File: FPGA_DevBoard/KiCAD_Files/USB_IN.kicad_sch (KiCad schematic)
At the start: 14 parts, among them J14 AWHW 14G-SMD, J3 USB4105-GF-A-060, SW1 219-8MST, U12 FT4232HPQ-REEL, X2 12MHz

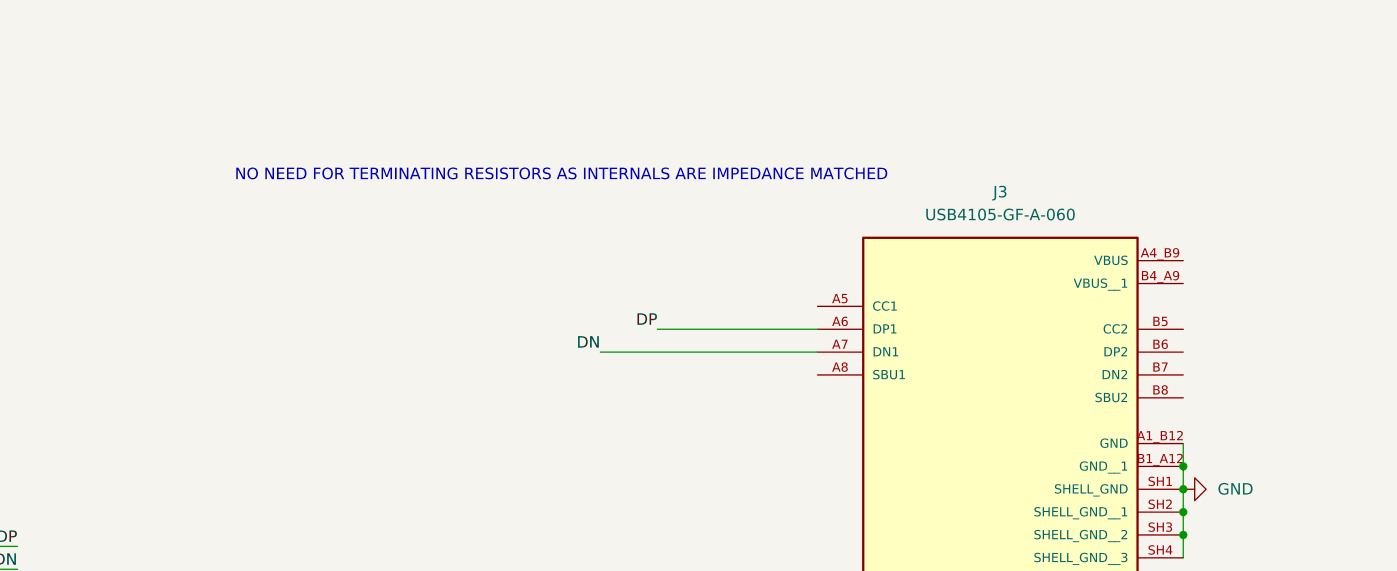
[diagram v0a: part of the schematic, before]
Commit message: ESD
Added ESD to the main USB programmer. Also added terminating resistors and test points. Also updated some planes to make sure everything was connected.
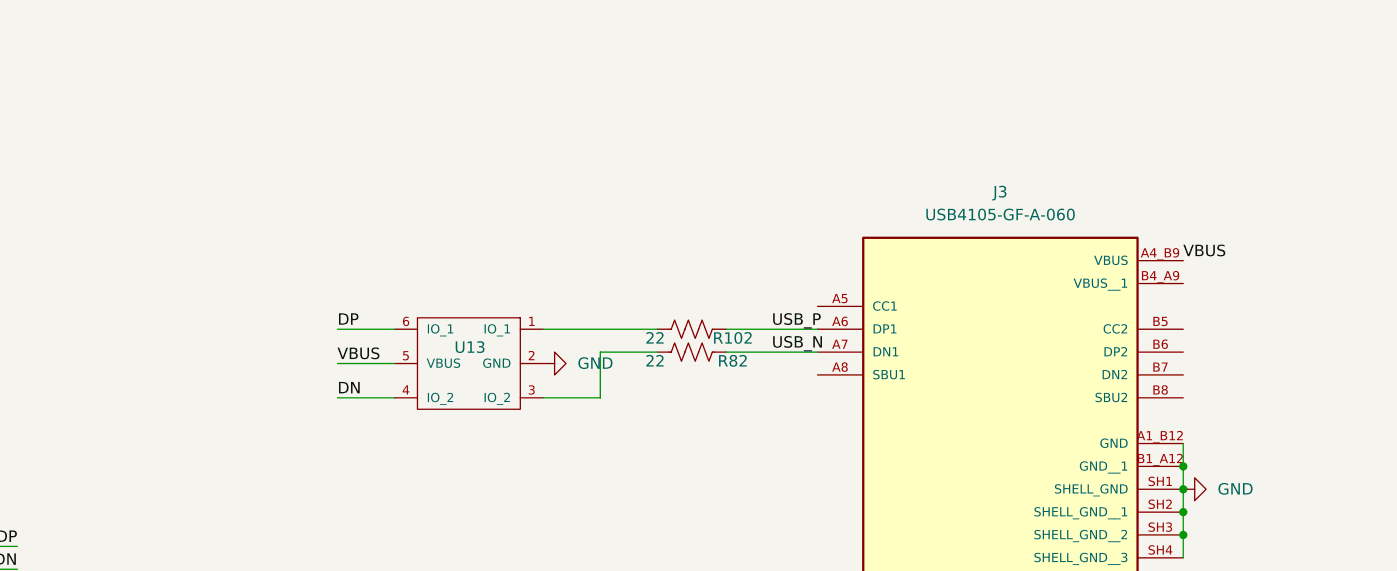
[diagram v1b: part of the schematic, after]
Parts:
- added R102, R82: 22, Resistor_SMD:R_0402_1005Metric, symbol Device:R_US
- added U13: USBLC6-2SC6, USB_HUB:SOT95P280X145-6N, symbol Test:USBLC6-2SC6
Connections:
- net DN: now also U13.4 (IO_2); no longer J3.A7 (DN1)
- net DP: now also U13.6 (IO_1); no longer J3.A6 (DP1)
- net GND: now also U13.2 (GND)
- net VBUS: now reaches J3.A4_B9 (VBUS)
- net VBUS: now also U13.5 (VBUS)
- new net: R82.2, U13.3 (IO_2)
- new net: R102.2, U13.1 (IO_1)
- new net USB_N: J3.A7 (DN1), R82.1
- new net USB_P: J3.A6 (DP1), R102.1
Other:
- note removed: "NO NEED FOR TERMINATING RESISTORS AS INTERNALS ARE IMPEDANCE MATCHED"

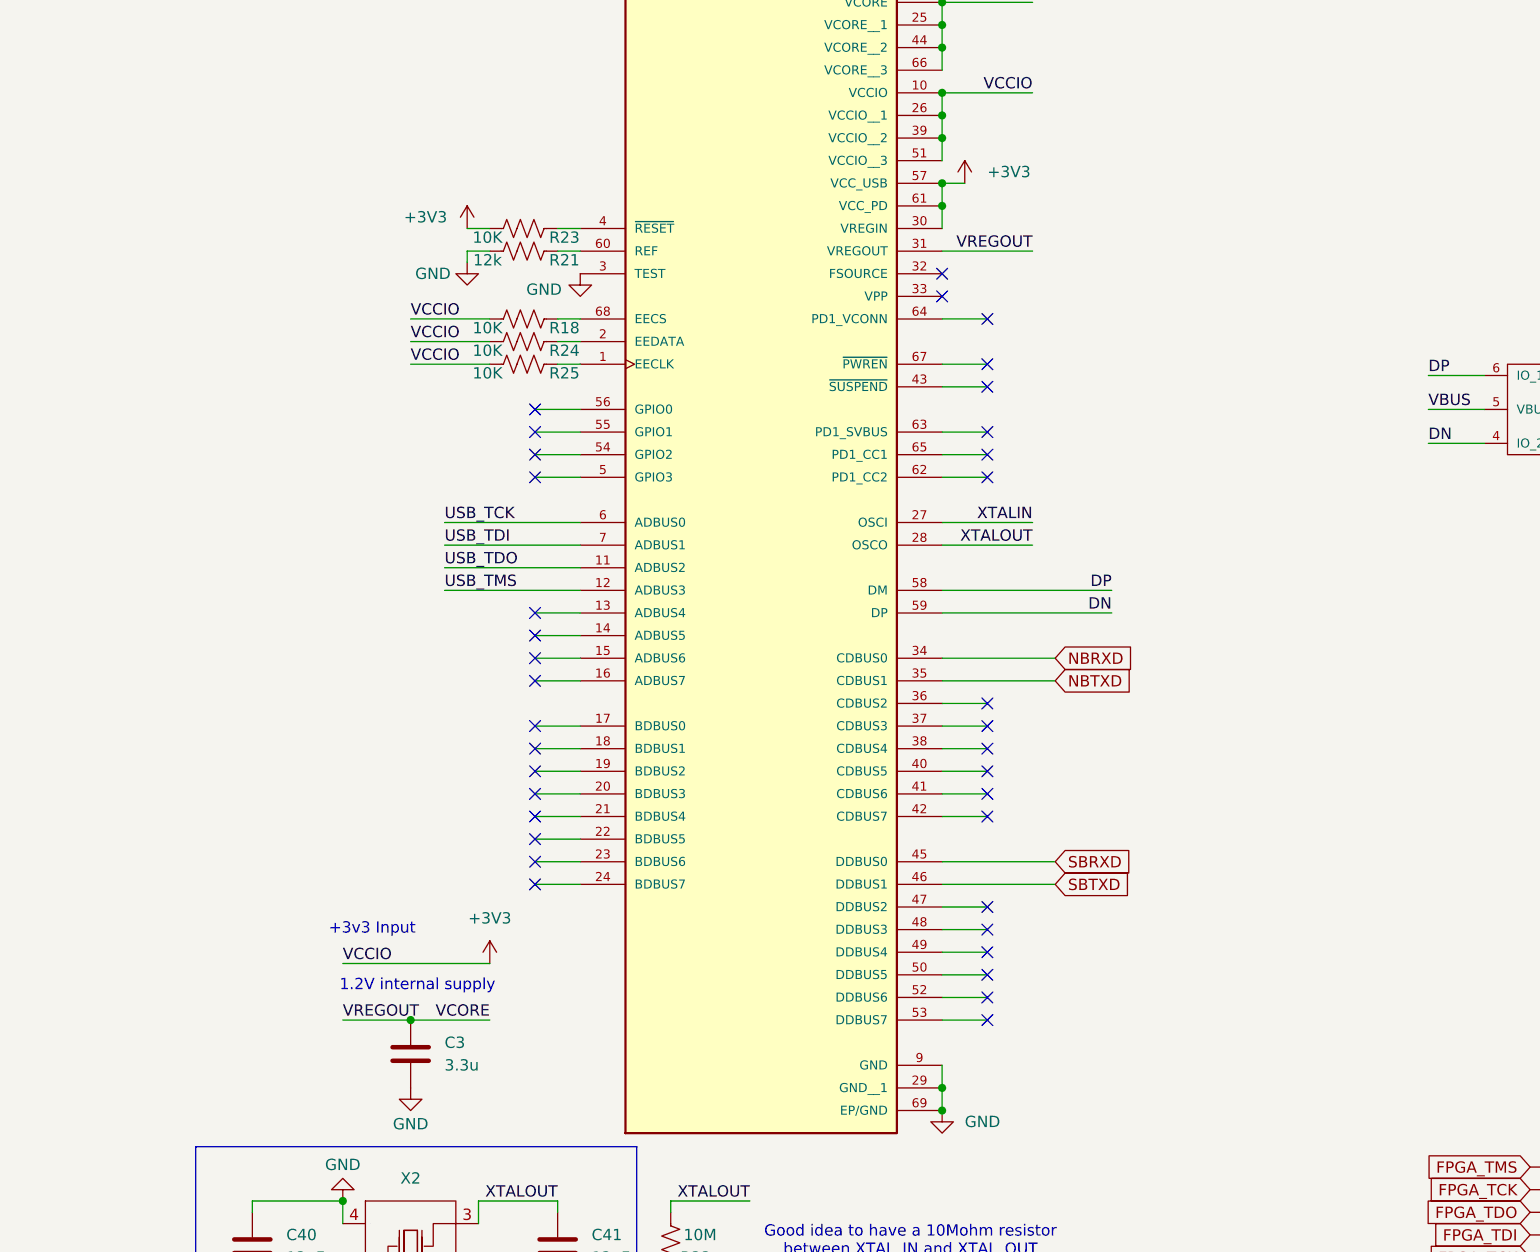
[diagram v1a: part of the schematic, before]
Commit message: FTDI
Added EEPROM To FTDI. Updated NB SPI bus. Added Debug LEDs to FTDI chip - PWREN and SUSPEND
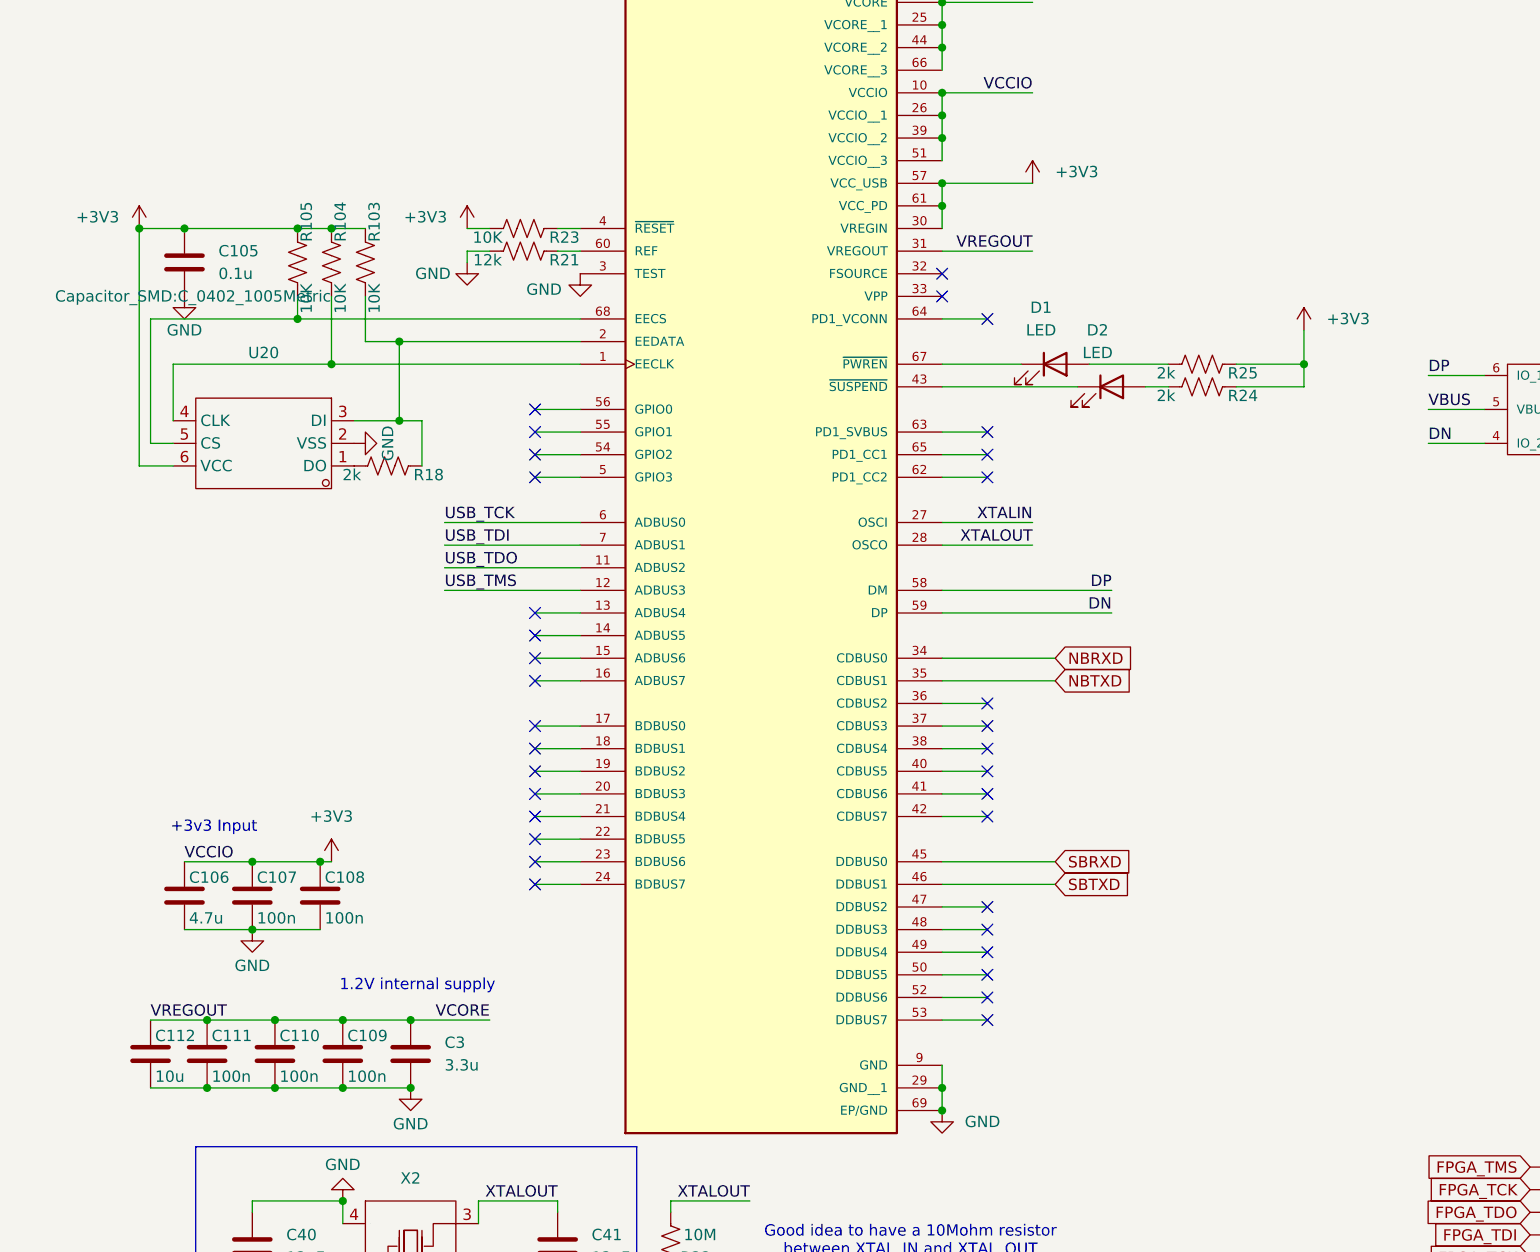
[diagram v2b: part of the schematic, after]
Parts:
- added C105: 0.1u, Capacitor_SMD:C_0402_1005Metric, symbol Device:C
- added C106: 4.7u, Capacitor_SMD:C_0603_1608Metric, symbol Device:C
- added C107, C108, C109, C110, C111: 100n, Capacitor_SMD:C_0603_1608Metric, symbol Device:C
- added C112: 10u, Capacitor_SMD:C_0603_1608Metric, symbol Device:C
- added D1, D2: LED, LED_SMD:LED_0603_1608Metric, symbol Device:LED
- added R103, R104, R105: 10K, Resistor_SMD:R_0402_1005Metric, symbol Device:R_US
- added U20: ~, FPGA&MCU:SOT-23-6_L2.9-W1.6-P0.95-LS2.8-BR, symbol FPGA&MCU:93LC56BT-I/OT
- R18, R24, R25: value 10K -> 2k
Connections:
- net +3V3: now also R24.1, R25.1, C105.1, C106.1, C107.1, C108.1, R103.1, R104.1, R105.1, U20.6 (VCC); no longer R18.2, R24.2, R25.2
- net GND: now also C105.2, C106.2, C107.2, C108.2, C109.2, C110.2, C111.2, C112.2, U20.2 (VSS)
- net VCORE: now also C109.1, C110.1, C111.1, C112.1
- net at U12.1 (EECLK): now also R104.2, U20.4 (CLK); no longer R25.1
- net at U12.2 (EEDATA): now also R18.1, R103.2, U20.3 (DI); no longer R24.1
- net at U12.43 (~{SUSPEND}): now also D2.1 (K)
- net at U12.67 (~{PWREN}): now also D1.1 (K)
- net at U12.68 (EECS): now also R105.2, U20.5 (CS); no longer R18.1
- new net: D2.2 (A), R24.2
- new net: R18.2, U20.1 (DO)
- new net: D1.2 (A), R25.2
- no-connect marks 38 -> 36

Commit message: Messed around with Traces again
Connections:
- net VBUS: now also J3.B4_A9 (VBUS__1)
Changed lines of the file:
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@@
+	(wire
+		(pts
+			(xy 252.73 68.58) (xy 252.73 71.12)
+		)
+		(stroke
+			(width 0)
+			(type default)
+		)
+	)
 	(wire
 		(pts

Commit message: Power Inductors
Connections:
- net ESD_N: now reaches R82.2, U13.3 (IO_2)
- net ESD_P: now reaches R102.2, U13.1 (IO_1)
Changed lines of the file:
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@@
+		)
+	)
+	(label "ESD_P"
+		(at 184.15 76.2 0)
+		(effects
+			(font
+				(size 1.27 1.27)
+			)
+			(justify left bottom)
 		)
 	)
@@
 		(effects
 			(font
+				(size 1.27 1.27)
+			)
+			(justify left bottom)
+		)
+	)
+	(label "ESD_N"
+		(at 184.15 83.82 0)
+		(effects
+			(font

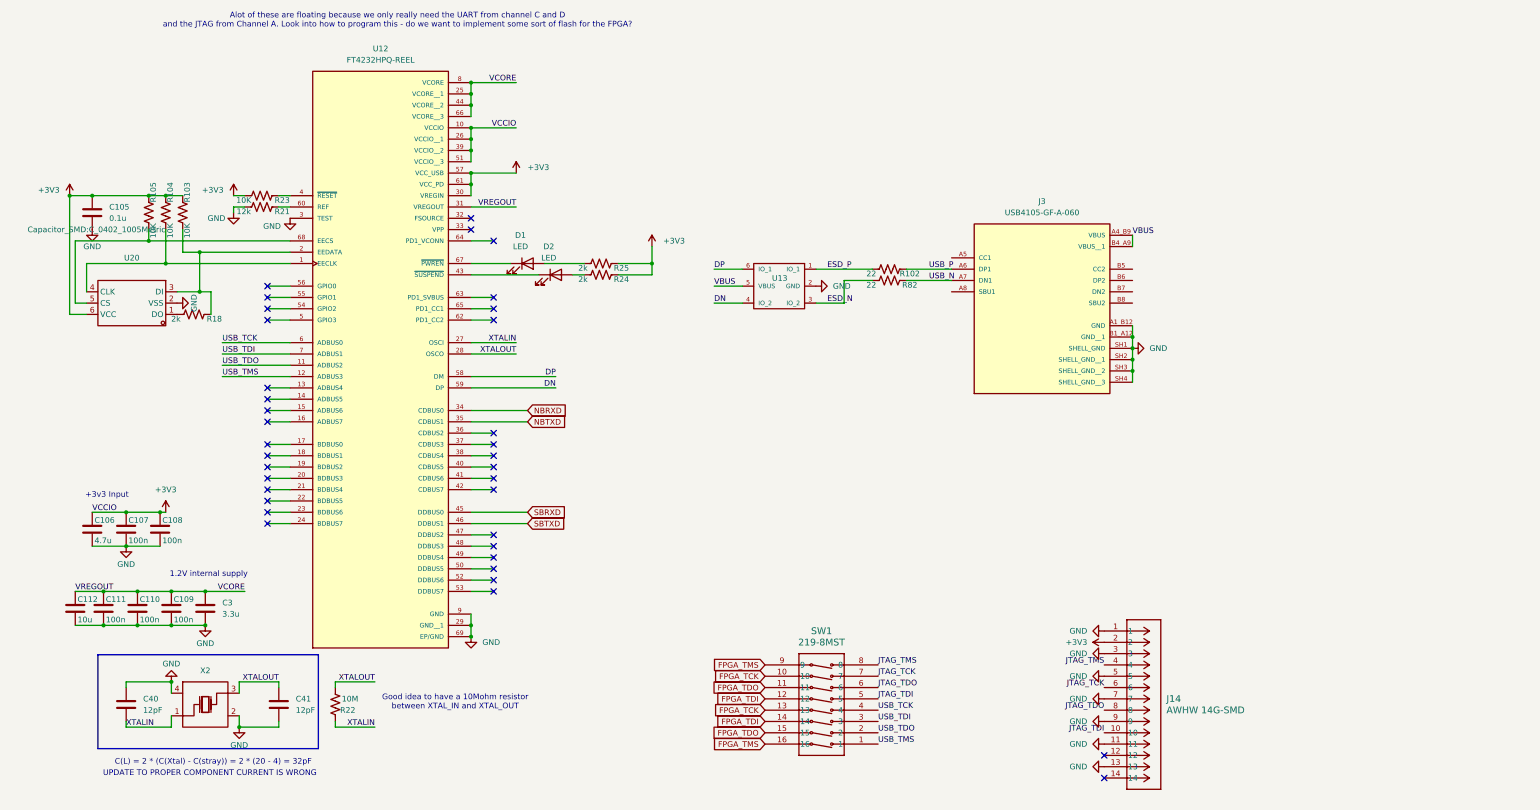
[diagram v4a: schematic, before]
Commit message: FTDI CHIP UPDATE
Updated all the PD stuff on the FTDI chip, also updated the USB to not be crossed, also moved the filtering caps towards the center of the chip.
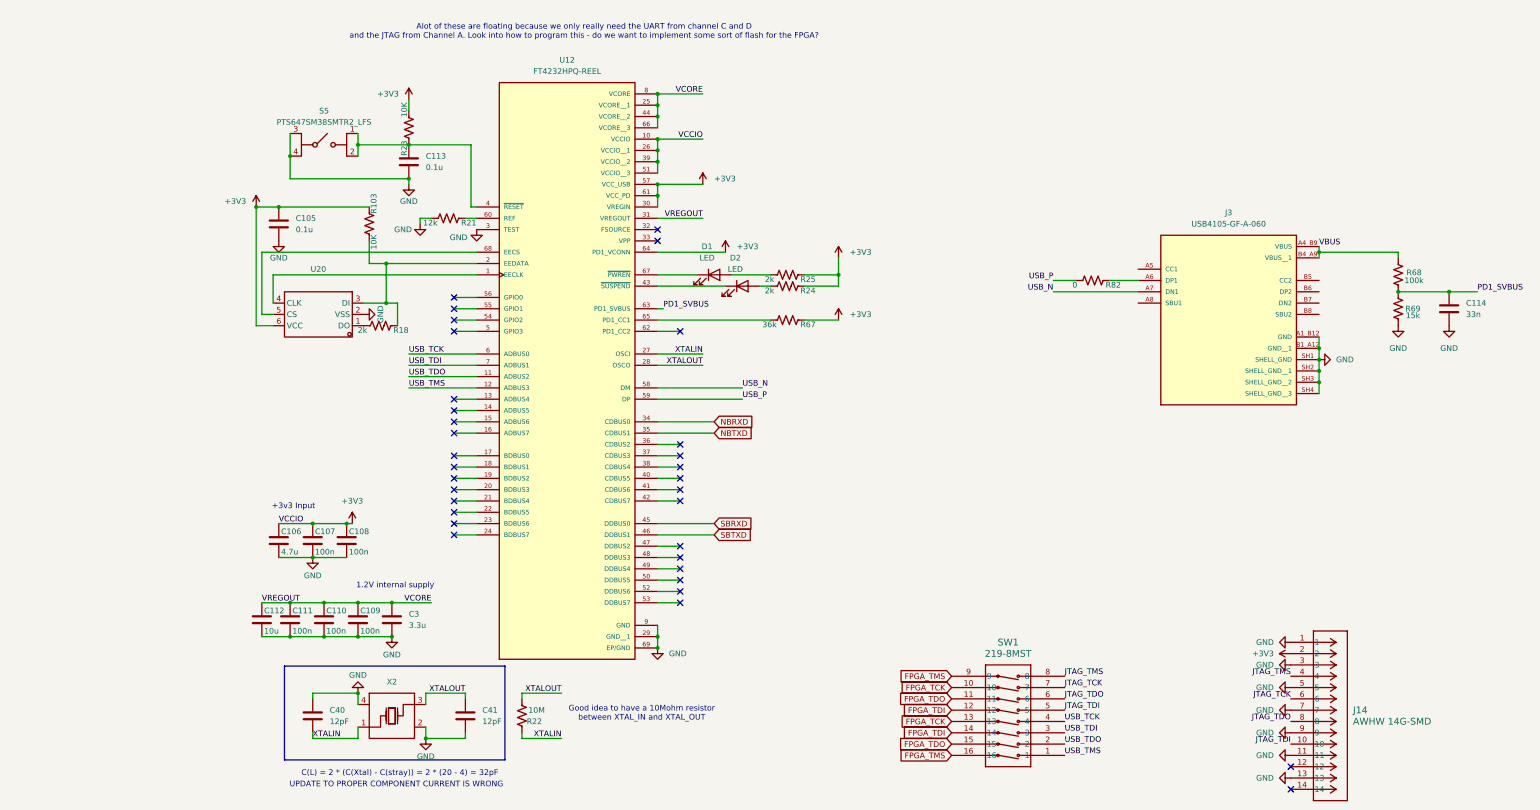
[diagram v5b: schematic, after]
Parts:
- removed R102: 22, Resistor_SMD:R_0402_1005Metric, symbol Device:R_US
- removed R104, R105: 10K, Resistor_SMD:R_0402_1005Metric, symbol Device:R_US
- removed U13: USBLC6-2SC6, USB_HUB:SOT95P280X145-6N, symbol Test:USBLC6-2SC6
- added C113: 0.1u, Capacitor_SMD:C_0402_1005Metric, symbol Device:C
- added C114: 33n, Capacitor_SMD:C_0402_1005Metric, symbol Device:C
- added R67: 36k, Resistor_SMD:R_0402_1005Metric, symbol Device:R_US
- added R68: 100k, Resistor_SMD:R_0402_1005Metric, symbol Device:R_US
- added R69: 15k, Resistor_SMD:R_0402_1005Metric, symbol Device:R_US
- added S5: PTS647SM38SMTR2_LFS, FPGA_Interface:PTS647SM38SMTR2LFS, symbol FPGA_Interface:PTS647SM38SMTR2_LFS
- R82: value 22 -> 0
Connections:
- net DN is gone; now on net USB_P: U12.59 (DP)
- net DP is gone; now on net USB_N: U12.58 (DM)
- net ESD_N is gone; now on net USB_P: R82.2
- net +3V3: now also U12.64 (PD1_VCONN), R67.1
- net GND: now also C113.2, C114.2, R69.1, S5.3 (COM_1), S5.4 (COM_2)
- net USB_N: no longer R82.1
- net USB_P: no longer J3.A6 (DP1)
- net VBUS: now also R68.2
- net at R23.1, U12.4 (~{RESET}): now also C113.1, S5.1 (NO_1), S5.2 (NO_2)
- net PD1_SVBUS: now reaches U12.63 (PD1_SVBUS)
- net PD1_SVBUS: now also C114.1, R68.1, R69.2
- net at U12.65 (PD1_CC1): now also R67.2
- new net: J3.A6 (DP1), R82.1
- no-connect marks 36 -> 33
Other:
- moved on the sheet: C105, C106, C107, C108, C109, C110, C111, C112, C3, C40, C41, D1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

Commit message: Updated the NBSB IO to not go to input only, need to change this on the layout. Updated the FPGA clk to go to a positive differential signal with MCRR - need to change on layout. Updated the USB-UART bridge to not have Regin grounded - need to change on layout.
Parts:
- U20: value ~ -> (none)
